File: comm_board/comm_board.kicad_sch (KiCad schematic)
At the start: 12 parts

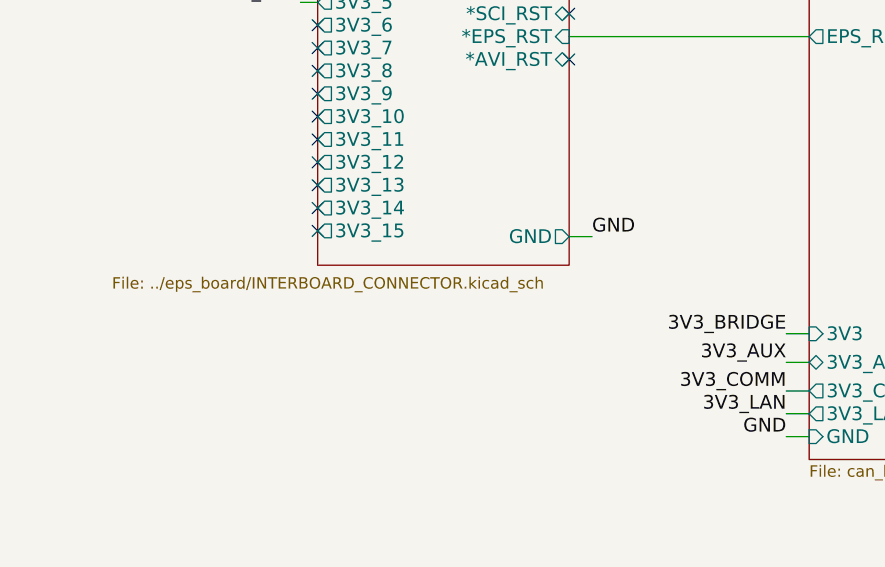
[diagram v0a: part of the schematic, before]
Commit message: move commonly used hierarchical sheets to common/sheets for easy reuse
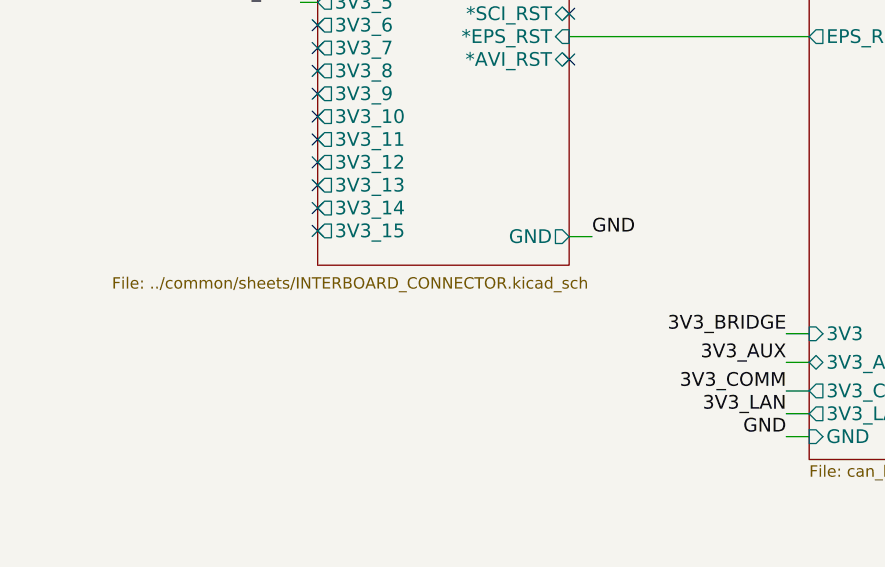
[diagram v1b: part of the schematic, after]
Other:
- sheet INTERBOARD_CONNECTOR2: file ../eps_board/INTERBOARD_CONNECTOR.kicad_sch -> ../common/sheets/INTERBOARD_CONNECTOR.kicad_sch
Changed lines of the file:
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@@
 			)
 		)
-		(property "Sheetfile" "../eps_board/INTERBOARD_CONNECTOR.kicad_sch"
+		(property "Sheetfile" "../common/sheets/INTERBOARD_CONNECTOR.kicad_sch"
 			(at 22.86 91.44 0)
 			(effects
@@
 		)
 		(instances
-			(project "openlst-hw"
+			(project "comm_board"
 				(path "/a863a5ec-a5d4-4f54-be53-e8c01d5e3ac4"
 					(page "6")
@@
 		)
 		(instances
-			(project "openlst-hw"
+			(project "comm_board"
 				(path "/a863a5ec-a5d4-4f54-be53-e8c01d5e3ac4"
 					(page "21")
@@
 		)
 		(instances
-			(project "openlst-hw"
+			(project "comm_board"
 				(path "/a863a5ec-a5d4-4f54-be53-e8c01d5e3ac4"
 					(page "6")
@@
 		)
 		(instances
-			(project "openlst-hw"
+			(project "comm_board"
 				(path "/a863a5ec-a5d4-4f54-be53-e8c01d5e3ac4"
 					(page "22")
@@
 		)
 		(instances
-			(project "openlst-hw"
+			(project "comm_board"
 				(path "/a863a5ec-a5d4-4f54-be53-e8c01d5e3ac4"
 					(page "2")

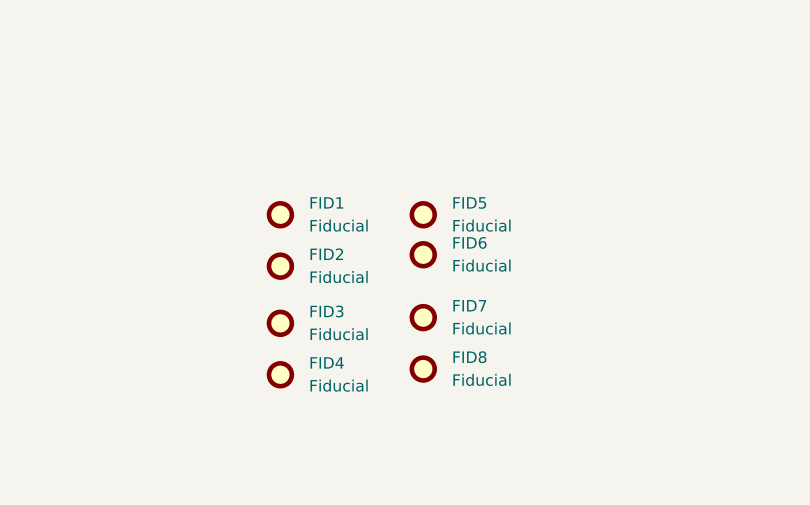
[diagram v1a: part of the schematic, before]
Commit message: absolute paths for includes of includes or the second level common/sheet will cause problems!
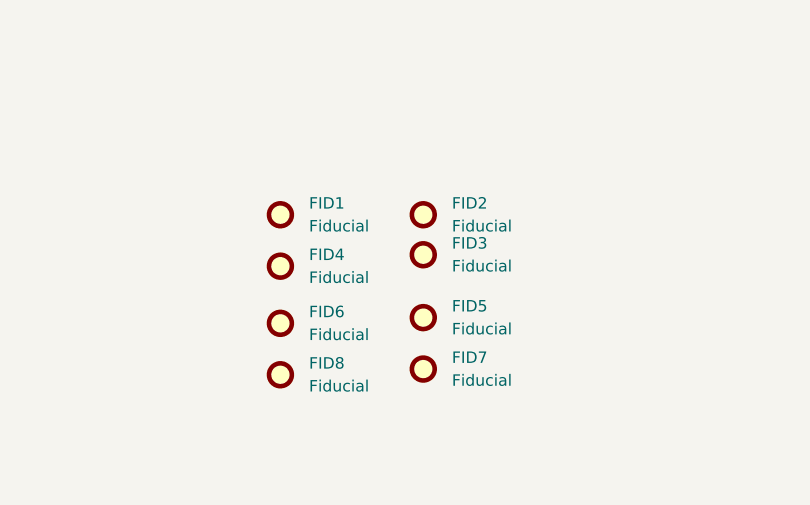
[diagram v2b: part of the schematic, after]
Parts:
- renumbered FID5 to FID2, FID6 to FID3, FID2 to FID4, FID7 to FID5, FID3 to FID6, FID8 to FID7, FID4 to FID8
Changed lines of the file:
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@@
 		(dnp no)
 		(fields_autoplaced yes)
-		(property "Reference" "FID6"
+		(property "Reference" "FID3"
 			(at 94.615 168.2749 0)
 			(effects
@@
 			(project "openlst-hw"
 				(path "/a863a5ec-a5d4-4f54-be53-e8c01d5e3ac4"
-					(reference "FID6")
+					(reference "FID3")
 					(unit 1)
 				)
@@
 		(dnp no)
 		(fields_autoplaced yes)
-		(property "Reference" "FID5"
+		(property "Reference" "FID2"
 			(at 94.615 163.8299 0)
 			(effects
@@
 			(project "openlst-hw"
 				(path "/a863a5ec-a5d4-4f54-be53-e8c01d5e3ac4"
-					(reference "FID5")
+					(reference "FID2")
 					(unit 1)
 				)
@@
 		(dnp no)
 		(fields_autoplaced yes)
-		(property "Reference" "FID7"
+		(property "Reference" "FID5"
 			(at 94.615 175.2599 0)
 			(effects
@@
 			(project "openlst-hw"
 				(path "/a863a5ec-a5d4-4f54-be53-e8c01d5e3ac4"
-					(reference "FID7")
+					(reference "FID5")
 					(unit 1)
 				)
@@
 		(dnp no)
 		(fields_autoplaced yes)
-		(property "Reference" "FID3"
+		(property "Reference" "FID6"
 			(at 78.74 175.8949 0)
 			(effects
@@
 			(project "openlst-hw"
 				(path "/a863a5ec-a5d4-4f54-be53-e8c01d5e3ac4"
-					(reference "FID3")
+					(reference "FID6")
 					(unit 1)
 				)
@@
 		(dnp no)
 		(fields_autoplaced yes)
-		(property "Reference" "FID8"
+		(property "Reference" "FID7"
 			(at 94.615 180.9749 0)
 			(effects
@@
 			(project "openlst-hw"
 				(path "/a863a5ec-a5d4-4f54-be53-e8c01d5e3ac4"
-					(reference "FID8")
+					(reference "FID7")
 					(unit 1)
 				)
@@
 		(dnp no)
 		(fields_autoplaced yes)
-		(property "Reference" "FID4"
+		(property "Reference" "FID8"
 			(at 78.74 181.6099 0)
 			(effects
@@
 			(project "openlst-hw"
 				(path "/a863a5ec-a5d4-4f54-be53-e8c01d5e3ac4"
-					(reference "FID4")
+					(reference "FID8")
 					(unit 1)
 				)
@@
 		(dnp no)
 		(fields_autoplaced yes)
-		(property "Reference" "FID2"
+		(property "Reference" "FID4"
 			(at 78.74 169.5449 0)
 			(effects
@@
 			(project "openlst-hw"
 				(path "/a863a5ec-a5d4-4f54-be53-e8c01d5e3ac4"
-					(reference "FID2")
-					(unit 1)
-				)
+					(reference "FID4")
+					(unit 1)
+				)
